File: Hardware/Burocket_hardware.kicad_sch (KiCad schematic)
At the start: 0 parts

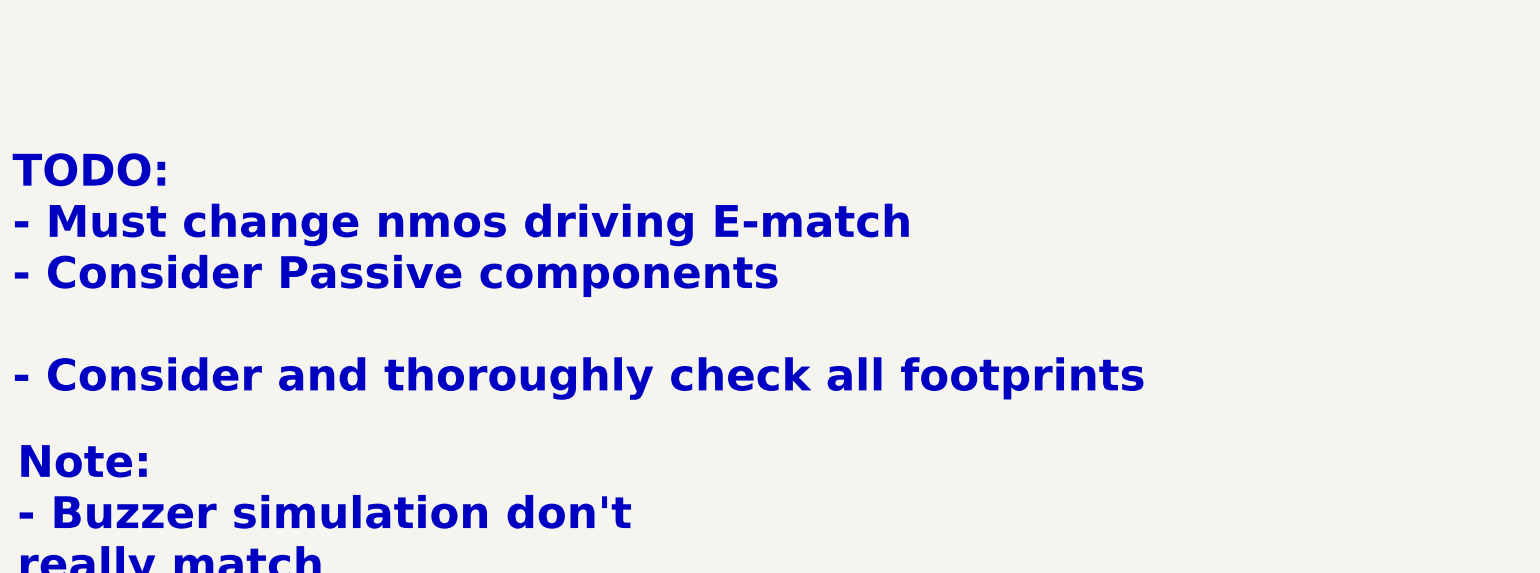
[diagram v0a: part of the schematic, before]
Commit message: Added MOSFET simulation files with official spice model
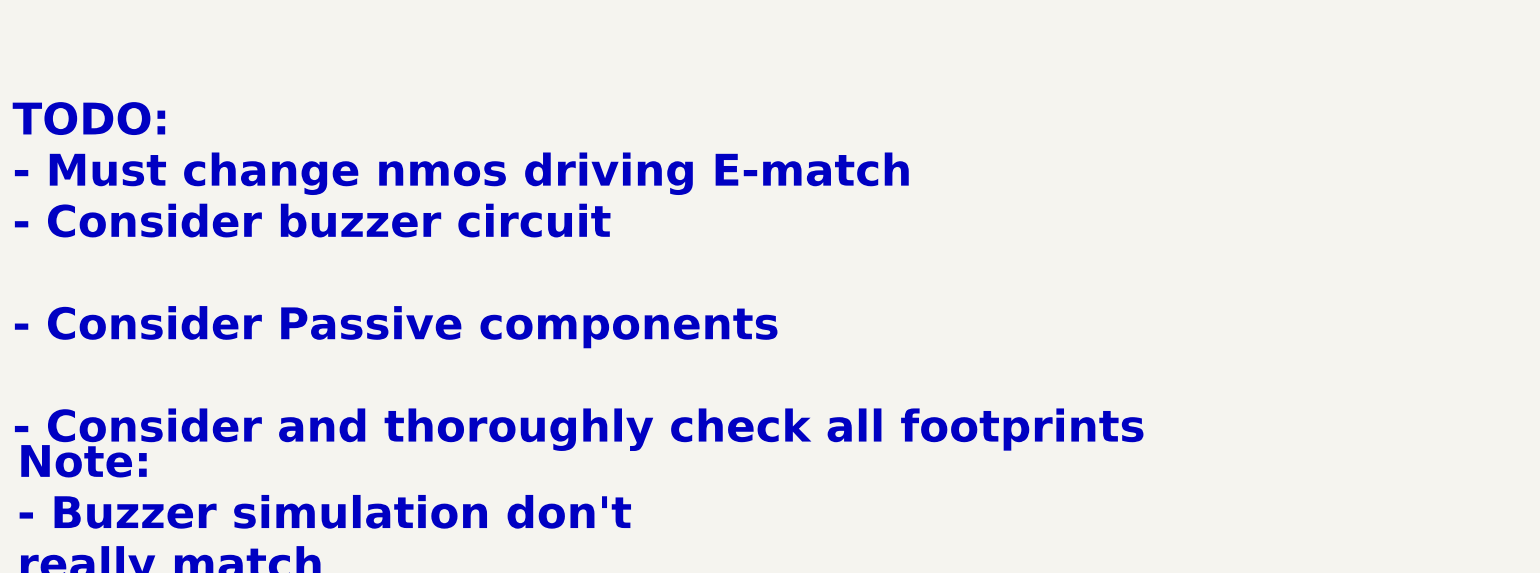
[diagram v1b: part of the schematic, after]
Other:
- note added: "TODO: - Must change nmos driving E-match - Consider buzzer circuit - Consider Passive components - Consider and thoroughly check all footprints"
- note removed: "TODO: - Must change nmos driving E-match - Consider Passive components - Consider and thoroughly check all footprints"
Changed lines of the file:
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@@
 		)
 	)
-	(text "TODO:\n- Must change nmos driving E-match\n- Consider Passive components\n\n- Consider and thoroughly check all footprints\n"
+	(text "TODO:\n- Must change nmos driving E-match\n- Consider buzzer circuit\n\n- Consider Passive components\n\n- Consider and thoroughly check all footprints\n"
 		(exclude_from_sim no)
 		(at -204.216 54.102 0)

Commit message: Purged heavy binaries and updated gitignore
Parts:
- added H1, H2, H3, H4: MountingHole_Pad, MountingHole:MountingHole_2.2mm_M2_Pad_Via, symbol Mechanical:MountingHole_Pad
- added Logo1: Burocket Logo, Burocket Logo:Burocket Logo, symbol Graphic:Logo_Open_Hardware_Large
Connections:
- new net GND: H1.1, H2.1, H3.1, H4.1
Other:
- note added: "Burocket Logo"
- note added: "Mounting Holes"
- note added: "To infinity and beyond!"
- note removed: "Note: - Buzzer simulation don't really match"
- note removed: "TODO: - Must change nmos driving E-match - Consider buzzer circuit - Consider Passive components - Consider and thoroughly check all footprints"
